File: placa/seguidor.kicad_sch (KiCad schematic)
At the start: 21 parts, among them J1 conn_bat, J2 conn_sensores, J3 conn_motor, J4 conn_pwm, J5 conn_icsp, SW1 SW_custom, SW2 btn_arranque, U1 ATmega328P-P, U2 LM7805_TO220, Y1 Crystal

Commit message: esquemático del diseño nuevo de la placa, falta el pcb
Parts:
- removed D2: 1N5819, Diode_THT:D_DO-41_SOD81_P10.16mm_Horizontal, symbol Diode:1N5819
- added C8, C9: 100u, Capacitor_THT:CP_Radial_D5.0mm_P2.00mm, symbol Device:C
- added D2, D3: 1N4007, Diode_THT:D_DO-41_SOD81_P10.16mm_Horizontal, symbol Diode:1N4007
- added J6: conn_bt, Connector_PinSocket_2.54mm:PinSocket_1x06_P2.54mm_Horizontal, symbol Connector_Generic:Conn_01x06
- added J7: jumper_bt, Connector_PinHeader_2.54mm:PinHeader_1x02_P2.54mm_Vertical, symbol Connector:Conn_01x02_Pin
- added R10, R11, R12, R13, R14, R15, R3, R4, R5, R6, R7, R8, R9: 3.3k, Resistor_THT:R_Axial_DIN0204_L3.6mm_D1.6mm_P5.08mm_Horizontal, symbol Device:R
- J1: footprint Connector_Molex:Molex_KK-396_A-41791-0002_1x02_P3.96mm_Vertical -> Connector_PinHeader_2.54mm:PinHeader_1x02_P2.54mm_Vertical
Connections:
- net +5V: now also J6.5 (Pin_5), R13.1
- net GND: now also C8.2, C9.2, J6.4 (Pin_4), R10.2, R11.2, R12.2, R15.1, R5.2, R8.2, R9.2; no longer J4.2 (Pin_2), J4.4 (Pin_4)
- net VCC: now also D2.1 (K), D3.2 (A), R3.1; no longer SW1.1
- net V_IN: now also D3.1 (K)
- net boton_largada: now also U1.4 (PD2); no longer U1.15 (PB1)
- net led_arranque: now also U1.6 (PD4); no longer U1.16 (PB2)
- net state_bt: now reaches U1.13 (PD7)
- net state_bt: now also J6.1 (Pin_1)
- net txd_bt: now reaches U1.2 (PD0)
- net txd_bt: now also J6.3 (Pin_3)
- net at U1.21 (AREF): now also C8.1
- net sensor_bat: now reaches U1.27 (PC4)
- net sensor_bat: now also C9.1, R4.2, R5.1
- net rxd_bt: now reaches U1.3 (PD1)
- net rxd_bt: now also R6.1
- net motor_der renamed motor_der1
- net motor_der1: now also U1.15 (PB1), R11.1; no longer U1.12 (PD6)
- net motor_izq renamed motor_izq1
- net motor_izq1: now also R9.1
- new net: J6.2 (Pin_2), R6.2, R7.1
- new net: R7.2, R8.1
- new net: J7.2 (Pin_2), R13.2
- new net: R3.2, R4.1
- new net: R14.1, R15.2
- new net: D2.2 (A), SW1.1
- new net key_bt: J6.6 (Pin_6), J7.1 (Pin_1), R14.2
- new net motor_der2: J4.4 (Pin_4), R12.1, U1.16 (PB2)
- new net motor_izq2: J4.2 (Pin_2), R10.1, U1.12 (PD6)
- no-connect marks 16 -> 9
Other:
- moved on the sheet: C2, C3, C5, C6, C7, D1, J2, J3, J4, J5, R2, SW2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

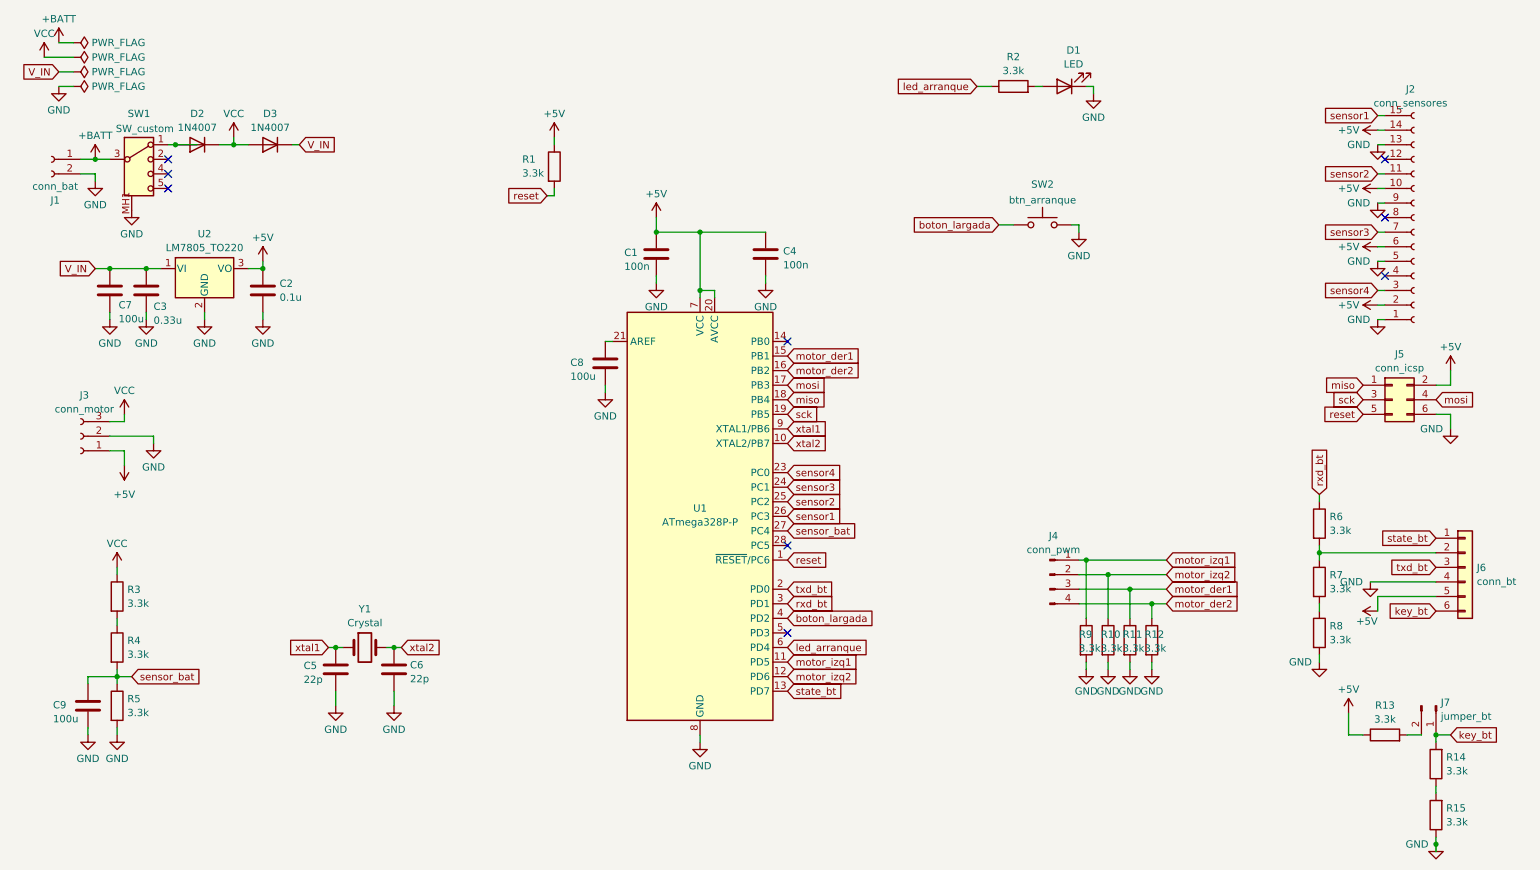
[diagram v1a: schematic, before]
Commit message: diseño de placa con bluetooth y motores en reversa
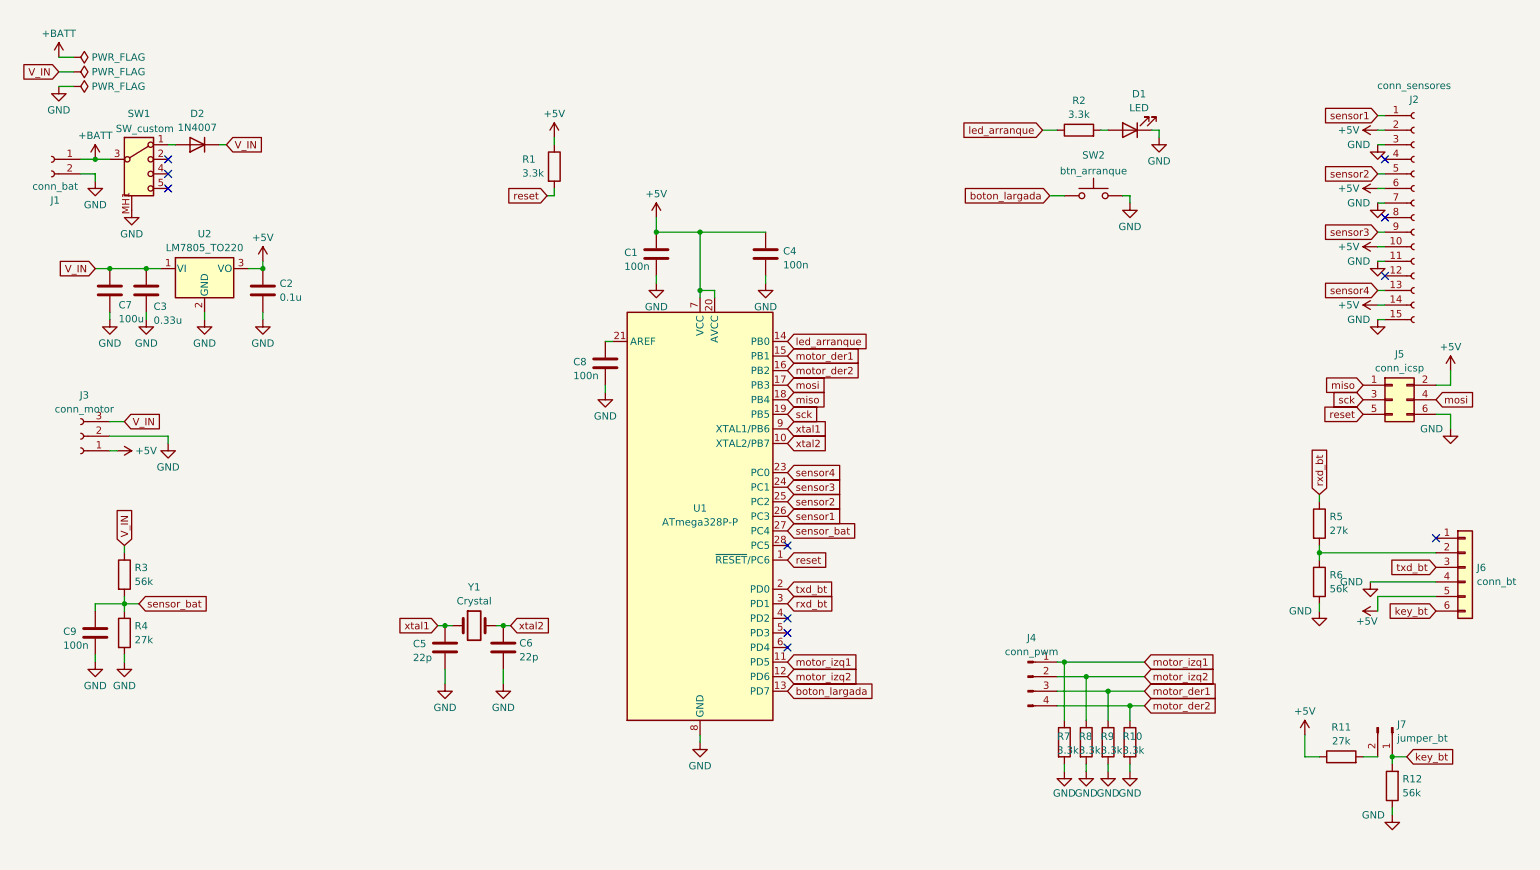
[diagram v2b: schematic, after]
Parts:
- removed D3: 1N4007, Diode_THT:D_DO-41_SOD81_P10.16mm_Horizontal, symbol Diode:1N4007
- removed R15, R4, R8: 3.3k, Resistor_THT:R_Axial_DIN0204_L3.6mm_D1.6mm_P5.08mm_Horizontal, symbol Device:R
- C8, C9: value 100u -> 100n; footprint Capacitor_THT:CP_Radial_D5.0mm_P2.00mm -> Capacitor_THT:C_Disc_D6.0mm_W2.5mm_P5.00mm
- J6: footprint Connector_PinSocket_2.54mm:PinSocket_1x06_P2.54mm_Horizontal -> Connector_PinSocket_2.54mm:PinSocket_1x06_P2.54mm_Vertical
- R11: renamed from R13; value 3.3k -> 27k; footprint Resistor_THT:R_Axial_DIN0204_L3.6mm_D1.6mm_P5.08mm_Horizontal -> Resistor_THT:R_Axial_DIN0207_L6.3mm_D2.5mm_P7.62mm_Horizontal
- R12: renamed from R14; value 3.3k -> 56k
- R3: value 3.3k -> 56k
- R4: renamed from R5; value 3.3k -> 27k; footprint Resistor_THT:R_Axial_DIN0204_L3.6mm_D1.6mm_P5.08mm_Horizontal -> Resistor_THT:R_Axial_DIN0207_L6.3mm_D2.5mm_P7.62mm_Horizontal
- R5: renamed from R6; value 3.3k -> 27k; footprint Resistor_THT:R_Axial_DIN0204_L3.6mm_D1.6mm_P5.08mm_Horizontal -> Resistor_THT:R_Axial_DIN0207_L6.3mm_D2.5mm_P7.62mm_Horizontal
- R6: renamed from R7; value 3.3k -> 56k
- renumbered R12 to R10, R9 to R7, R10 to R8, R11 to R9
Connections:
- net VCC is gone; now on net V_IN: D2.1 (K), J3.3 (Pin_3), R3.1
- net GND: now also J2.11 (Pin_11), J2.15 (Pin_15), J2.3 (Pin_3), J2.7 (Pin_7), R12.1, R6.2; no longer J2.1 (Pin_1), J2.13 (Pin_13), J2.5 (Pin_5), J2.9 (Pin_9)
- net boton_largada: now also U1.13 (PD7); no longer U1.4 (PD2)
- net led_arranque: now also U1.14 (PB0); no longer U1.6 (PD4)
- net sensor1: now also J2.1 (Pin_1); no longer J2.15 (Pin_15)
- net sensor2: now also J2.5 (Pin_5); no longer J2.11 (Pin_11)
- net sensor3: now also J2.9 (Pin_9); no longer J2.7 (Pin_7)
- net sensor4: now also J2.13 (Pin_13); no longer J2.3 (Pin_3)
- net sensor_bat: now also R3.2
- net state_bt: no longer names the net of J6.1 (Pin_1)
- net state_bt: no longer U1.13 (PD7)
- no-connect marks 9 -> 11
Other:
- moved on the sheet: C5, C6, D1, J4, J7, R10, R11, R12, R2, R3, R4, R7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
